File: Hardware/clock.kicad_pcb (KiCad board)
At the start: 2 copper layers, 98 x 55 mm, 58 parts, among them J1 Conn_02x05_Counter_Clockwise, J2 Conn_01x02_Male, J3 USB_B_Micro, J4 Barrel_Jack, Q1 2N7002ET1G, SW1 SW_Push, SW2 SW_Push, SW3 SW_Push, U1 STM32F103C8Tx, U2 UA78M33CDCY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

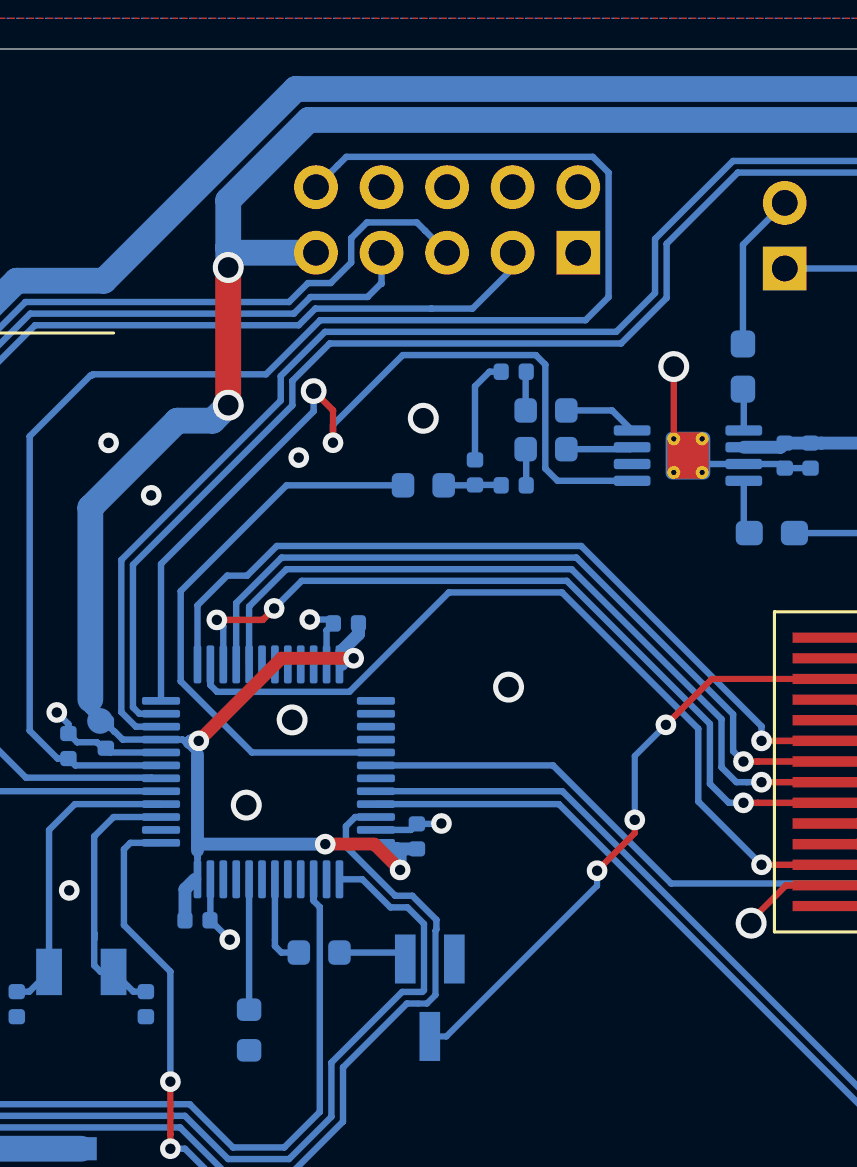
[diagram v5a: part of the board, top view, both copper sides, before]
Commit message: Small changes to code after populating board. Hardware should be unchanged.
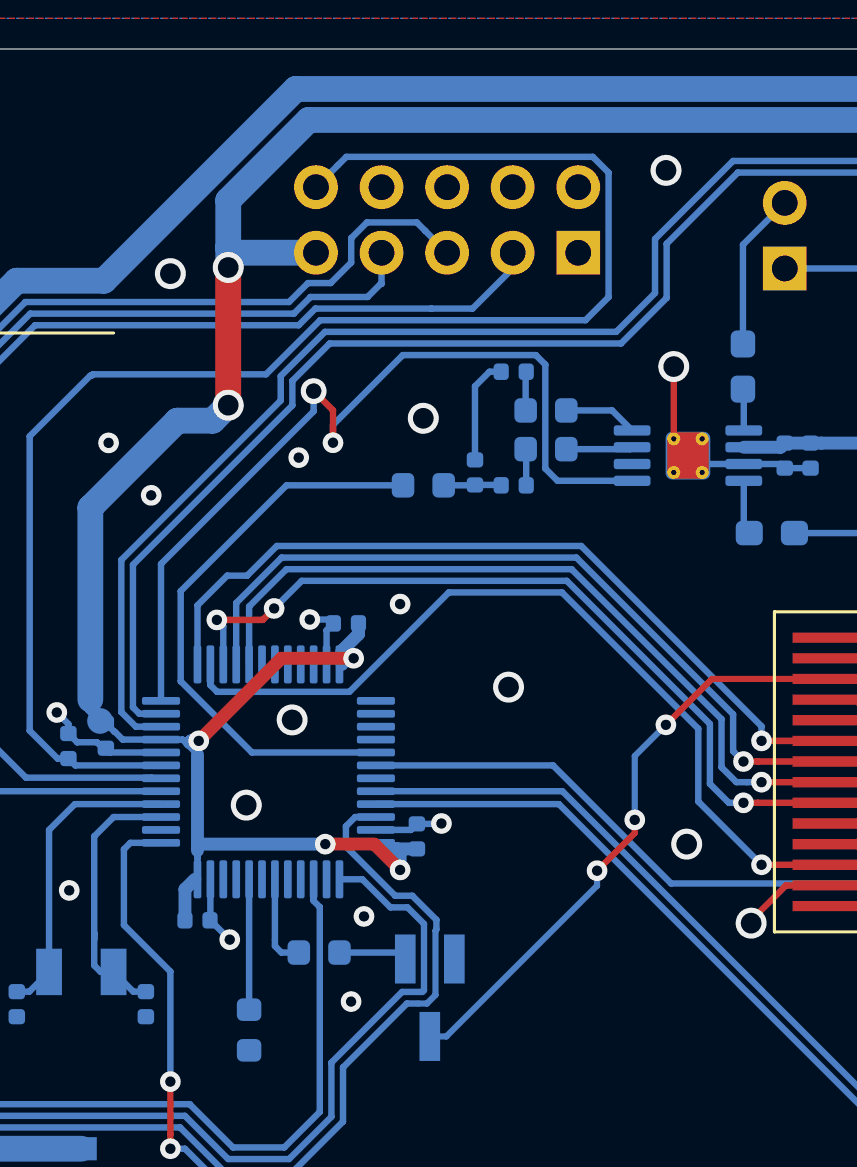
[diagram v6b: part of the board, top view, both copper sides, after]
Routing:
- net GND: vias 32 -> 38
